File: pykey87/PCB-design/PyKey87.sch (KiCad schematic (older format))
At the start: 303 parts, among them J1 USB_C_Receptacle_USB2.0, J2 Conn_01x03, SW1 SW_SPST, SW2 SW_SPDT, U1 CherryMX_LTST-A683CEGBW, U10 CherryMX_LTST-A683CEGBW, U100 RP2040, U101 USBLC6-2SC6, U102 W25Q128JVS, U103 AMS1117-3.3, U11 CherryMX_LTST-A683CEGBW, U12 CherryMX_LTST-A683CEGBW, U13 CherryMX_LTST-A683CEGBW, U14 CherryMX_LTST-A683CEGBW, U15 CherryMX_LTST-A683CEGBW, U16 CherryMX_LTST-A683CEGBW, U17 CherryMX_LTST-A683CEGBW, U18 CherryMX_LTST-A683CEGBW, U19 CherryMX_LTST-A683CEGBW, U2 CherryMX_LTST-A683CEGBW, U20 CherryMX_LTST-A683CEGBW, U21 CherryMX_LTST-A683CEGBW, U22 CherryMX_LTST-A683CEGBW, U23 CherryMX_LTST-A683CEGBW, U24 CherryMX_LTST-A683CEGBW, U25 CherryMX_LTST-A683CEGBW, U26 CherryMX_LTST-A683CEGBW, U27 CherryMX_LTST-A683CEGBW, U28 CherryMX_LTST-A683CEGBW, U29 CherryMX_LTST-A683CEGBW, U3 CherryMX_LTST-A683CEGBW, U30 CherryMX_LTST-A683CEGBW, U31 CherryMX_LTST-A683CEGBW, U32 CherryMX_LTST-A683CEGBW, U33 CherryMX_LTST-A683CEGBW, U34 CherryMX_LTST-A683CEGBW, U35 CherryMX_LTST-A683CEGBW, U36 CherryMX_LTST-A683CEGBW, U37 CherryMX_LTST-A683CEGBW, U38 CherryMX_LTST-A683CEGBW, U39 CherryMX_LTST-A683CEGBW, U4 CherryMX_LTST-A683CEGBW, U40 CherryMX_LTST-A683CEGBW, U41 CherryMX_LTST-A683CEGBW, U42 CherryMX_LTST-A683CEGBW, U43 CherryMX_LTST-A683CEGBW, U44 CherryMX_LTST-A683CEGBW, U45 CherryMX_LTST-A683CEGBW, U46 CherryMX_LTST-A683CEGBW, U47 CherryMX_LTST-A683CEGBW, U48 CherryMX_LTST-A683CEGBW, U49 CherryMX_LTST-A683CEGBW, U5 CherryMX_LTST-A683CEGBW, U50 CherryMX_LTST-A683CEGBW, U51 CherryMX_LTST-A683CEGBW, U52 CherryMX_LTST-A683CEGBW, U53 CherryMX_LTST-A683CEGBW, U54 CherryMX_LTST-A683CEGBW, U55 CherryMX_LTST-A683CEGBW, U56 CherryMX_LTST-A683CEGBW, U57 CherryMX_LTST-A683CEGBW, U58 CherryMX_LTST-A683CEGBW, U59 CherryMX_LTST-A683CEGBW, U6 CherryMX_LTST-A683CEGBW, U60 CherryMX_LTST-A683CEGBW, U61 CherryMX_LTST-A683CEGBW, U62 CherryMX_LTST-A683CEGBW, U63 CherryMX_LTST-A683CEGBW, U64 CherryMX_LTST-A683CEGBW, U65 CherryMX_LTST-A683CEGBW, U66 CherryMX_LTST-A683CEGBW, U67 CherryMX_LTST-A683CEGBW, U68 CherryMX_LTST-A683CEGBW, U69 CherryMX_LTST-A683CEGBW, U7 CherryMX_LTST-A683CEGBW, U70 CherryMX_LTST-A683CEGBW, U71 CherryMX_LTST-A683CEGBW, U72 CherryMX_LTST-A683CEGBW, U73 CherryMX_LTST-A683CEGBW, U74 CherryMX_LTST-A683CEGBW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

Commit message: Move boot/run and reset to edge
Also cleanup, renaming, and adding a second I2C header.
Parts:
- added H8: MountingHole_Pad, MountingHole:MountingHole_2.2mm_M2_Pad, symbol Mechanical:MountingHole_Pad
- added J3: Conn_01x04, Connector_JST:JST_SH_BM04B-SRSS-TB_1x04-1MP_P1.00mm_Vertical, symbol Connector_Generic:Conn_01x04
- J1: symbol PyKey60-rescue:USB_C_Receptacle_USB2.0-Connector -> PyKey87-rescue:USB_C_Receptacle_USB2.0-Connector-PyKey87-rescue
- U101: symbol PyKey60-rescue:USBLC6-2SC6-Power_Protection -> PyKey87-rescue:USBLC6-2SC6-Power_Protection-PyKey87-rescue
- U102: symbol PyKey60-rescue:W25Q128JVS-Memory_Flash -> PyKey87-rescue:W25Q128JVS-Memory_Flash-PyKey87-rescue
- renumbered C88 to C1, C97 to C10, C13 to C100, C14 to C101, C15 to C102, C16 to C103, C98 to C11, C99 to C12, C100 to C13, C101 to C14, C102 to C15, C103 to C16, C89 to C2, C90 to C3, C91 to C4, C92 to C5, C93 to C6, C94 to C7, C95 to C8, C1 to C88, C2 to C89, C96 to C9, C3 to C90, C4 to C91, C5 to C92, C6 to C93, C7 to C94, C8 to C95, C9 to C96, C10 to C97, C11 to C98, C12 to C99
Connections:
- net labels added: +3.3V
- wire segments 1417 -> 1404
- no-connect marks 7 -> 15
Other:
- moved on the sheet: H1

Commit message: Working on issues
https://github.com/jpconstantineau/PyKey60/issues/3
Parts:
- added H10, H9: MountingHole, lib.pretty:MountingHole_1.152mm, symbol Mechanical:MountingHole
- added J4: AudioJack4, Connector_Audio:Jack_3.5mm_PJ320D_Horizontal, symbol Connector:AudioJack4
- added J5: Conn_01x04, Connector_PinHeader_2.54mm:PinHeader_1x04_P2.54mm_Vertical, symbol Connector_Generic:Conn_01x04
- J3: Note (none) -> Qwiic connector
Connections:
- net +3V3: now also J4.T, J5.2 (Pin_2)
- net GND: now also J4.S, J5.1 (Pin_1)
- net I2C1_SCL: now also J4.R2, J5.3 (Pin_3)
- net I2C1_SDA: now also J4.R1, J5.4 (Pin_4)
- net ROW0: now also D75.1 (K), D76.1 (K), D77.1 (K)
- net ROW1: now also D78.1 (K), D79.1 (K), D80.1 (K)
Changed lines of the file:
@@
 Sheet 1 1
 Title "PyKey87 RP2040"
-Date "2021-09-16"
+Date "2021-11-14"
 Rev "1.0"
-Comp "Pierre Constantineau (JPConstantineau)"
+Comp "Pierre Constantineau (JPConstantineau) & nitronarcosis"
 Comment1 "License: CERN-OHL-W (CERN OHL v2)"
 Comment2 "https://github.com/nitronarcosis/PyKey87"
@@
 $EndComp
 Wire Wire Line
-	17850 1850 19100 1850
-Wire Wire Line
-	17850 2600 19100 2600
-Wire Wire Line
 	3550 1000 3550 1300
 $Comp
@@
 F 2 "Connector_JST:JST_SH_BM04B-SRSS-TB_1x04-1MP_P1.00mm_Vertical" H 7750 12450 50  0001 C CNN
 F 3 "~" H 7750 12450 50  0001 C CNN
+F 4 "Qwiic connector" H 8450 12250 50  0000 R BNN "Note"
 	1    7750 12450
 	1    0    0    -1
@@
 Wire Wire Line
 	17500 1600 17500 2350
+Text GLabel 7550 11900 0    60   Input ~ 0
+I2C1_SDA
+Text GLabel 7550 11800 0    60   Input ~ 0
+I2C1_SCL
+Text GLabel 7350 11200 0    60   Input ~ 0
+I2C1_SCL
+$Comp
+L Connector:AudioJack4 J4
+U 1 1 62305BE4
+P 7550 11200
+F 0 "J4" H 7220 11083 50  0000 R CNN
+F 1 "AudioJack4" H 7220 11174 50  0000 R CNN
+F 2 "Connector_Audio:Jack_3.5mm_PJ320D_Horizontal" H 7550 11200 50  0001 C CNN
+F 3 "~" H 7550 11200 50  0001 C CNN
+	1    7550 11200
+	-1   0    0    1
+$EndComp
+Text GLabel 7350 11100 0    60   Input ~ 0
+I2C1_SDA
+$Comp
+L power:GND #PWR0300
+U 1 1 62F64508
+P 7350 11300
+F 0 "#PWR0300" H 7350 11050 50  0001 C CNN
+F 1 "GND" V 7355 11172 50  0000 R CNN
+F 2 "" H 7350 11300 50  0001 C CNN
+F 3 "" H 7350 11300 50  0001 C CNN
+	1    7350 11300
+	0    1    1    0
+$EndComp
+$Comp
+L power:+3.3V #PWR0301
+U 1 1 62F67571
+P 7350 11000
+F 0 "#PWR0301" H 7350 10850 50  0001 C CNN
+F 1 "+3.3V" V 7365 11128 50  0000 L CNN
+F 2 "" H 7350 11000 50  0001 C CNN
+F 3 "" H 7350 11000 50  0001 C CNN
+	1    7350 11000
+	0    -1   -1   0
+$EndComp
+$Comp
+L power:+3.3V #PWR0302
+U 1 1 631E332A
+P 7550 11700
+F 0 "#PWR0302" H 7550 11550 50  0001 C CNN
+F 1 "+3.3V" V 7565 11828 50  0000 L CNN
+F 2 "" H 7550 11700 50  0001 C CNN
+F 3 "" H 7550 11700 50  0001 C CNN
+	1    7550 11700
+	0    -1   -1   0
+$EndComp
+$Comp
+L power:GND #PWR0303
+U 1 1 631E671F
+P 7550 11600
+F 0 "#PWR0303" H 7550 11350 50  0001 C CNN
+F 1 "GND" V 7555 11472 50  0000 R CNN
+F 2 "" H 7550 11600 50  0001 C CNN
+F 3 "" H 7550 11600 50  0001 C CNN
+	1    7550 11600
+	0    1    1    0
+$EndComp
+Connection ~ 17650 1850
+Wire Wire Line
+	17650 1850 19100 1850
+Wire Wire Line
+	17650 2600 19100 2600
+Connection ~ 17650 2600
+$Comp
+L Mechanical:MountingHole H9
+U 1 1 643992E6
+P 20850 8150
+F 0 "H9" H 20950 8241 50  0000 L CNN
+F 1 "MountingHole" H 20950 8150 50  0000 L CNN
+F 2 "lib.pretty:MountingHole_1.152mm" H 20850 8150 50  0001 C CNN
+F 3 "~" H 20850 8150 50  0001 C CNN
+F 4 "JLCPCB Tooling Hole" H 20950 8059 50  0000 L CNN "Note"
+	1    20850 8150
+	1    0    0    -1
+$EndComp
+$Comp
+L Mechanical:MountingHole H10
+U 1 1 646109EF
+P 20850 8450
+F 0 "H10" H 20950 8541 50  0000 L CNN
+F 1 "MountingHole" H 20950 8450 50  0000 L CNN
+F 2 "lib.pretty:MountingHole_1.152mm" H 20850 8450 50  0001 C CNN
+F 3 "~" H 20850 8450 50  0001 C CNN
+F 4 "JLCPCB Tooling Hole" H 20950 8359 50  0000 L CNN "Note"
+	1    20850 8450
+	1    0    0    -1
+$EndComp
+$Comp
+L Connector_Generic:Conn_01x04 J5
+U 1 1 62304B28
+P 7750 11700
+F 0 "J5" H 7830 11737 50  0000 L CNN
+F 1 "Conn_01x04" H 7830 11646 50  0000 L CNN
+F 2 "Connector_PinHeader_2.54mm:PinHeader_1x04_P2.54mm_Vertical" H 7750 11700 50  0001 C CNN
+F 3 "~" H 7750 11700 50  0001 C CNN
+F 4 "OLED Connector" H 7830 11555 50  0000 L TNN "Note"
+	1    7750 11700
+	1    0    0    -1
+$EndComp
 $EndSCHEMATC

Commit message: working on issue 2
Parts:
- added H7: MountingHole, lib.pretty:KB_BlueMicro, symbol Mechanical:MountingHole
- J3: footprint Connector_JST:JST_SH_BM04B-SRSS-TB_1x04-1MP_P1.00mm_Vertical -> Connector_JST:JST_SH_SM04B-SRSS-TB_1x04-1MP_P1.00mm_Horizontal
- SW1: footprint Button_Switch_SMD:SW_Push_SPST_NO_Alps_SKRK -> Button_Switch_SMD:Panasonic_EVQPUL_EVQPUC
- U74, U77, U80, U83, U84, U87: footprint CherryMX_PCB_KailhSocket_StabWireTop_LTST-A683CEGBW-Rotated-HS:CherryMX_2.00u_PCB_KailhSocket_StabWireTop_LTST-A683CEGB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 -> CherryMX_PCB_KailhSocket_LTST-A683CEGBW-Rotated-HS:CherryMX_1.00u_PCB_KailhSocket_LTST-A683CEGBW-Rotated-HS
- renumbered H7 to H11
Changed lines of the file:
@@
 F 0 "U74" H 18350 2085 50  0000 C CNN
 F 1 "CherryMX_LTST-A683CEGBW" H 18350 1994 50  0000 C CNN
-F 2 "CherryMX_PCB_KailhSocket_StabWireTop_LTST-A683CEGBW-Rotated-HS:CherryMX_2.00u_PCB_KailhSocket_StabWireTop_LTST-A683CEGBW-Rotated-HS" H 18350 1600 50  0001 C CNN
+F 2 "CherryMX_PCB_KailhSocket_LTST-A683CEGBW-Rotated-HS:CherryMX_1.00u_PCB_KailhSocket_LTST-A683CEGBW-Rotated-HS" H 18350 1600 50  0001 C CNN
 F 3 "" H 18350 1600 50  0001 C CNN
 	1    18350 1700
@@
 F 0 "U77" H 22350 2085 50  0000 C CNN
 F 1 "CherryMX_LTST-A683CEGBW" H 22350 1994 50  0000 C CNN
-F 2 "CherryMX_PCB_KailhSocket_StabWireTop_LTST-A683CEGBW-Rotated-HS:CherryMX_2.00u_PCB_KailhSocket_StabWireTop_LTST-A683CEGBW-Rotated-HS" H 22350 1600 50  0001 C CNN
+F 2 "CherryMX_PCB_KailhSocket_LTST-A683CEGBW-Rotated-HS:CherryMX_1.00u_PCB_KailhSocket_LTST-A683CEGBW-Rotated-HS" H 22350 1600 50  0001 C CNN
 F 3 "" H 22350 1600 50  0001 C CNN
 	1    22350 1700
@@
 F 0 "U80" H 22350 2835 50  0000 C CNN
 F 1 "CherryMX_LTST-A683CEGBW" H 22350 2744 50  0000 C CNN
-F 2 "CherryMX_PCB_KailhSocket_StabWireTop_LTST-A683CEGBW-Rotated-HS:CherryMX_2.00u_PCB_KailhSocket_StabWireTop_LTST-A683CEGBW-Rotated-HS" H 22350 2350 50  0001 C CNN
+F 2 "CherryMX_PCB_KailhSocket_LTST-A683CEGBW-Rotated-HS:CherryMX_1.00u_PCB_KailhSocket_LTST-A683CEGBW-Rotated-HS" H 22350 2350 50  0001 C CNN
 F 3 "" H 22350 2350 50  0001 C CNN
 	1    22350 2450
@@
 F 0 "U83" H 22350 3535 50  0000 C CNN
 F 1 "CherryMX_LTST-A683CEGBW" H 22350 3444 50  0000 C CNN
-F 2 "CherryMX_PCB_KailhSocket_StabWireTop_LTST-A683CEGBW-Rotated-HS:CherryMX_2.00u_PCB_KailhSocket_StabWireTop_LTST-A683CEGBW-Rotated-HS" H 22350 3050 50  0001 C CNN
+F 2 "CherryMX_PCB_KailhSocket_LTST-A683CEGBW-Rotated-HS:CherryMX_1.00u_PCB_KailhSocket_LTST-A683CEGBW-Rotated-HS" H 22350 3050 50  0001 C CNN
 F 3 "" H 22350 3050 50  0001 C CNN
 	1    22350 3150
@@
 F 0 "U84" H 21100 5035 50  0000 C CNN
 F 1 "CherryMX_LTST-A683CEGBW" H 21100 4944 50  0000 C CNN
-F 2 "CherryMX_PCB_KailhSocket_StabWireTop_LTST-A683CEGBW-Rotated-HS:CherryMX_2.00u_PCB_KailhSocket_StabWireTop_LTST-A683CEGBW-Rotated-HS" H 21100 4550 50  0001 C CNN
+F 2 "CherryMX_PCB_KailhSocket_LTST-A683CEGBW-Rotated-HS:CherryMX_1.00u_PCB_KailhSocket_LTST-A683CEGBW-Rotated-HS" H 21100 4550 50  0001 C CNN
 F 3 "" H 21100 4550 50  0001 C CNN
 	1    21100 4650
@@
 F 0 "U87" H 22350 5785 50  0000 C CNN
 F 1 "CherryMX_LTST-A683CEGBW" H 22350 5694 50  0000 C CNN
-F 2 "CherryMX_PCB_KailhSocket_StabWireTop_LTST-A683CEGBW-Rotated-HS:CherryMX_2.00u_PCB_KailhSocket_StabWireTop_LTST-A683CEGBW-Rotated-HS" H 22350 5300 50  0001 C CNN
+F 2 "CherryMX_PCB_KailhSocket_LTST-A683CEGBW-Rotated-HS:CherryMX_1.00u_PCB_KailhSocket_LTST-A683CEGBW-Rotated-HS" H 22350 5300 50  0001 C CNN
 F 3 "" H 22350 5300 50  0001 C CNN
 	1    22350 5400
@@
 F 0 "SW1" H 8200 10435 50  0000 C CNN
 F 1 "SW_SPST" H 8200 10344 50  0000 C CNN
-F 2 "Button_Switch_SMD:SW_Push_SPST_NO_Alps_SKRK" H 8200 10200 50  0001 C CNN
+F 2 "Button_Switch_SMD:Panasonic_EVQPUL_EVQPUC" H 8200 10200 50  0001 C CNN
 F 3 "~" H 8200 10200 50  0001 C CNN
 	1    8200 10200
@@
 I2C1_SCL
 $Comp
-L Mechanical:MountingHole_Pad H7
+L Mechanical:MountingHole_Pad H11
 U 1 1 61B6C89D
 P 20550 7000
-F 0 "H7" H 20650 7049 50  0000 L CNN
+F 0 "H11" H 20650 7049 50  0000 L CNN
 F 1 "MountingHole_Pad" H 20650 6958 50  0000 L CNN
 F 2 "MountingHole:MountingHole_2.2mm_M2_Pad" H 20550 7000 50  0001 C CNN
@@
 F 0 "J3" H 7830 12442 50  0000 L CNN
 F 1 "Conn_01x04" H 7830 12351 50  0000 L CNN
-F 2 "Connector_JST:JST_SH_BM04B-SRSS-TB_1x04-1MP_P1.00mm_Vertical" H 7750 12450 50  0001 C CNN
+F 2 "Connector_JST:JST_SH_SM04B-SRSS-TB_1x04-1MP_P1.00mm_Horizontal" H 7750 12450 50  0001 C CNN
 F 3 "~" H 7750 12450 50  0001 C CNN
 F 4 "Qwiic connector" H 8450 12250 50  0000 R BNN "Note"
@@
 	1    0    0    -1
 $EndComp
+$Comp
+L Mechanical:MountingHole H7
+U 1 1 61C2B0D9
+P 19250 8500
+F 0 "H7" H 19350 8546 50  0000 L CNN
+F 1 "MountingHole" H 19350 8455 50  0000 L CNN
+F 2 "lib.pretty:KB_BlueMicro" H 19250 8500 50  0001 C CNN
+F 3 "~" H 19250 8500 50  0001 C CNN
+	1    19250 8500
+	1    0    0    -1
+$EndComp

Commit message: Initial upload of plate, fixing issues
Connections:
- net ROW5: no longer D87.1 (K)
- net at D86.2 (A), U86.1: now also D87.1 (K)
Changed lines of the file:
@@
 $EndComp
 Wire Wire Line
-	21650 5550 21650 5300
-Wire Wire Line
 	21650 2600 21650 2350
 Wire Wire Line
@@
 Wire Wire Line
 	20700 5300 20800 5300
-Connection ~ 20400 5550
-Wire Wire Line
-	20400 5550 21650 5550
 Wire Wire Line
 	20400 5550 20400 5300
@@
 	1    0    0    -1
 $EndComp
+Wire Wire Line
+	21650 5300 21650 4950
+Wire Wire Line
+	21650 4950 20700 4950
+Wire Wire Line
+	20700 4950 20700 5300
+Connection ~ 20700 5300
 $EndSCHEMATC

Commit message: Move D87 for better fit
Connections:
- net ROW5: now also D87.1 (K)
- net at D86.2 (A), U86.1: no longer D87.1 (K)
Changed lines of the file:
@@
 $EndComp
 Wire Wire Line
-	21650 5300 21650 4950
+	21650 5300 21650 5550
 Wire Wire Line
-	21650 4950 20700 4950
-Wire Wire Line
-	20700 4950 20700 5300
-Connection ~ 20700 5300
+	21650 5550 20400 5550
+Connection ~ 20400 5550
 $EndSCHEMATC

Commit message: Misc fixes to schematic, PCB, and plates
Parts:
- J1: symbol PyKey87-rescue:USB_C_Receptacle_USB2.0-Connector-PyKey87-rescue -> Connector:USB_C_Receptacle_USB2.0
- U101: symbol PyKey87-rescue:USBLC6-2SC6-Power_Protection-PyKey87-rescue -> Power_Protection:USBLC6-2SC6
- U102: symbol PyKey87-rescue:W25Q128JVS-Memory_Flash-PyKey87-rescue -> Memory_Flash:W25Q128JVS
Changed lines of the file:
@@
 EESchema Schematic File Version 4
-LIBS:PyKey87-cache
-EELAYER 29 0
+EELAYER 30 0
 EELAYER END
 $Descr User 24213 14370
@@
 $EndComp
 $Comp
-L PyKey87-rescue:W25Q128JVS-Memory_Flash-PyKey87-rescue U102
+L Memory_Flash:W25Q128JVS U102
 U 1 1 613CF811
 P 6100 7550
@@
 $EndComp
 $Comp
-L PyKey87-rescue:USBLC6-2SC6-Power_Protection-PyKey87-rescue U101
+L Power_Protection:USBLC6-2SC6 U101
 U 1 1 613D38EF
 P 2950 7150
@@
 NoConn ~ 1800 7750
 $Comp
-L PyKey87-rescue:USB_C_Receptacle_USB2.0-Connector-PyKey87-rescue J1
+L Connector:USB_C_Receptacle_USB2.0 J1
 U 1 1 613B693C
 P 1200 7150

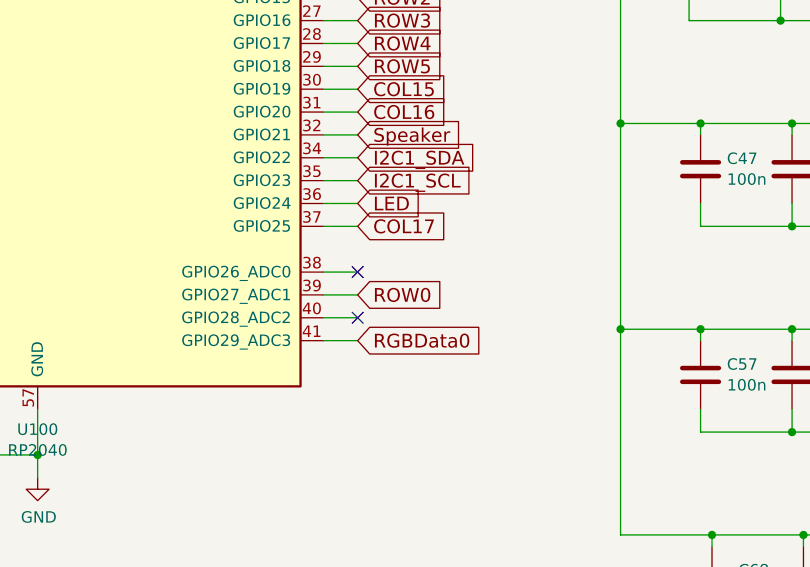
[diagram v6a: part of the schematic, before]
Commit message: Moved Row0, and rotated stabilizers in plate
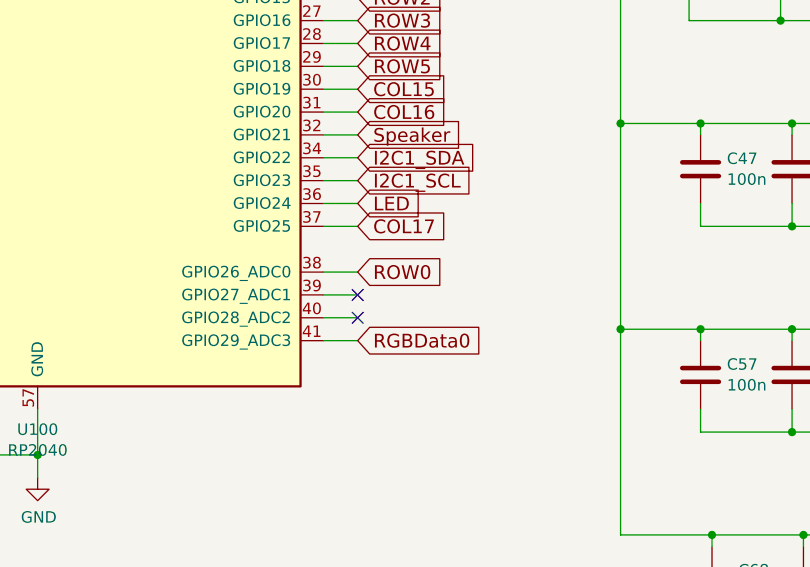
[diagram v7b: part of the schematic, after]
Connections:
- net ROW0: now also U100.38 (GPIO26_ADC0); no longer U100.39 (GPIO27_ADC1)
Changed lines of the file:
@@
 	11150 10600 11000 10600
 NoConn ~ 11150 11000
-NoConn ~ 11150 10800
 Wire Wire Line
 	1050 1850 3700 1850
@@
 Text GLabel 11150 9500 2    60   Input ~ 0
 ROW1
-Text GLabel 11150 10900 2    60   Input ~ 0
+Text GLabel 11150 10800 2    60   Input ~ 0
 ROW0
 Text GLabel 11150 10600 2    60   Input ~ 0
@@
 	21650 5550 20400 5550
 Connection ~ 20400 5550
+NoConn ~ 11150 10900
 $EndSCHEMATC

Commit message: Generate production files
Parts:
- D1, D10, D11, D12, D13, D14, D15, D16, D17, D18, D19, D2, D20, D21, D22, D23, D24, D25, D26, D27, D28, D29, D3, D30, D31, D32, D33, D34, D35, D36, D37, D38, D39, D4, D40, D41, D42, D43, D44, D45, D46, D47, D48, D49, D5, D50, D51, D52, D53, D54, D55, D56, D57, D58, D59, D6, D60, D61, D62, D63, D64, D65, D66, D67, D68, D69, D7, D70, D71, D72, D73, D74, D75, D76, D77, D78, D79, D8, D80, D81, D82, D83, D84, D85, D86, D87, D9: LCSC (none) -> C81598
- D101: LCSC C90692 -> C2286
- J4: LCSC (none) -> C521460
- LS1: LCSC (none) -> C6186
- SW1: LCSC (none) -> C388883
- Y1: LCSC C93114 -> C9002
